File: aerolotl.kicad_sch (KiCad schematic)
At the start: 0 parts

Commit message: final rev1
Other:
- sheet Igniters renamed Igniter
- sheet External ports: added PWM1, PWM2; removed none
- sheet MCU ports: added PWM1, PWM2; removed none
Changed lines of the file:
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@@
 	(bus
 		(pts
-			(xy 250.19 140.335) (xy 294.005 140.335)
+			(xy 250.19 138.43) (xy 294.005 138.43)
 		)
 		(stroke
@@
 	(bus
 		(pts
-			(xy 250.19 138.43) (xy 294.005 138.43)
+			(xy 250.19 136.525) (xy 294.005 136.525)
 		)
 		(stroke
@@
 	(wire
 		(pts
-			(xy 250.19 147.955) (xy 294.005 147.955)
+			(xy 250.19 149.225) (xy 294.005 149.225)
 		)
 		(stroke
@@
 		)
 	)
+	(wire
+		(pts
+			(xy 250.19 140.97) (xy 294.005 140.97)
+		)
+		(stroke
+			(width 0)
+			(type default)
+		)
+	)
 	(bus
 		(pts
@@
 	(wire
 		(pts
-			(xy 250.19 146.05) (xy 294.005 146.05)
+			(xy 250.19 147.32) (xy 294.005 147.32)
 		)
 		(stroke
@@
 		(pts
 			(xy 127 52.07) (xy 127 90.805)
+		)
+		(stroke
+			(width 0)
+			(type default)
+		)
+	)
+	(wire
+		(pts
+			(xy 250.19 143.51) (xy 294.005 143.51)
 		)
 		(stroke
@@
 			(color 0 0 0 0.0000)
 		)
-		(property "Sheetname" "Igniters"
+		(property "Sheetname" "Igniter"
 			(at 294.005 211.3784 0)
 			(effects
@@
 		)
 		(pin "I2C2{SDA, SCL}" bidirectional
+			(at 294.005 136.525 180)
+			(effects
+				(font
+					(size 1.27 1.27)
+				)
+				(justify left)
+			)
+		)
+		(pin "I2C4{SDA, SCL}" bidirectional
 			(at 294.005 138.43 180)
-			(effects
-				(font
-					(size 1.27 1.27)
-				)
-				(justify left)
-			)
-		)
-		(pin "I2C4{SDA, SCL}" bidirectional
-			(at 294.005 140.335 180)
 			(effects
 				(font
@@
 		)
 		(pin "USART3_TARGET_RX" input
-			(at 294.005 146.05 180)
+			(at 294.005 147.32 180)
 			(effects
 				(font
@@
 		)
 		(pin "USART3_TARGET_TX" output
-			(at 294.005 147.955 180)
+			(at 294.005 149.225 180)
+			(effects
+				(font
+					(size 1.27 1.27)
+				)
+				(justify left)
+			)
+		)
+		(pin "PWM1" input
+			(at 294.005 140.97 180)
+			(effects
+				(font
+					(size 1.27 1.27)
+				)
+				(justify left)
+			)
+		)
+		(pin "PWM2" input
+			(at 294.005 143.51 180)
 			(effects
 				(font
@@
 		)
 		(pin "I2C2{SDA, SCL}" input
+			(at 250.19 136.525 0)
+			(effects
+				(font
+					(size 1.27 1.27)
+				)
+				(justify right)
+			)
+		)
+		(pin "I2C4{SDA, SCL}" input
 			(at 250.19 138.43 0)
-			(effects
-				(font
-					(size 1.27 1.27)
-				)
-				(justify right)
-			)
-		)
-		(pin "I2C4{SDA, SCL}" input
-			(at 250.19 140.335 0)
 			(effects
 				(font
@@
 		)
 		(pin "USART3_RX" input
-			(at 250.19 146.05 0)
+			(at 250.19 147.32 0)
 			(effects
 				(font
@@
 		)
 		(pin "USART3_TX" output
-			(at 250.19 147.955 0)
+			(at 250.19 149.225 0)
 			(effects
 				(font
@@
 			(effects
 				(font
+					(size 1.27 1.27)
+				)
+				(justify right)
+			)
+		)
+		(pin "PWM1" output
+			(at 250.19 140.97 0)
+			(effects
+				(font
+					(size 1.27 1.27)
+				)
+				(justify right)
+			)
+		)
+		(pin "PWM2" output
+			(at 250.19 143.51 0)
+			(effects
+				(font

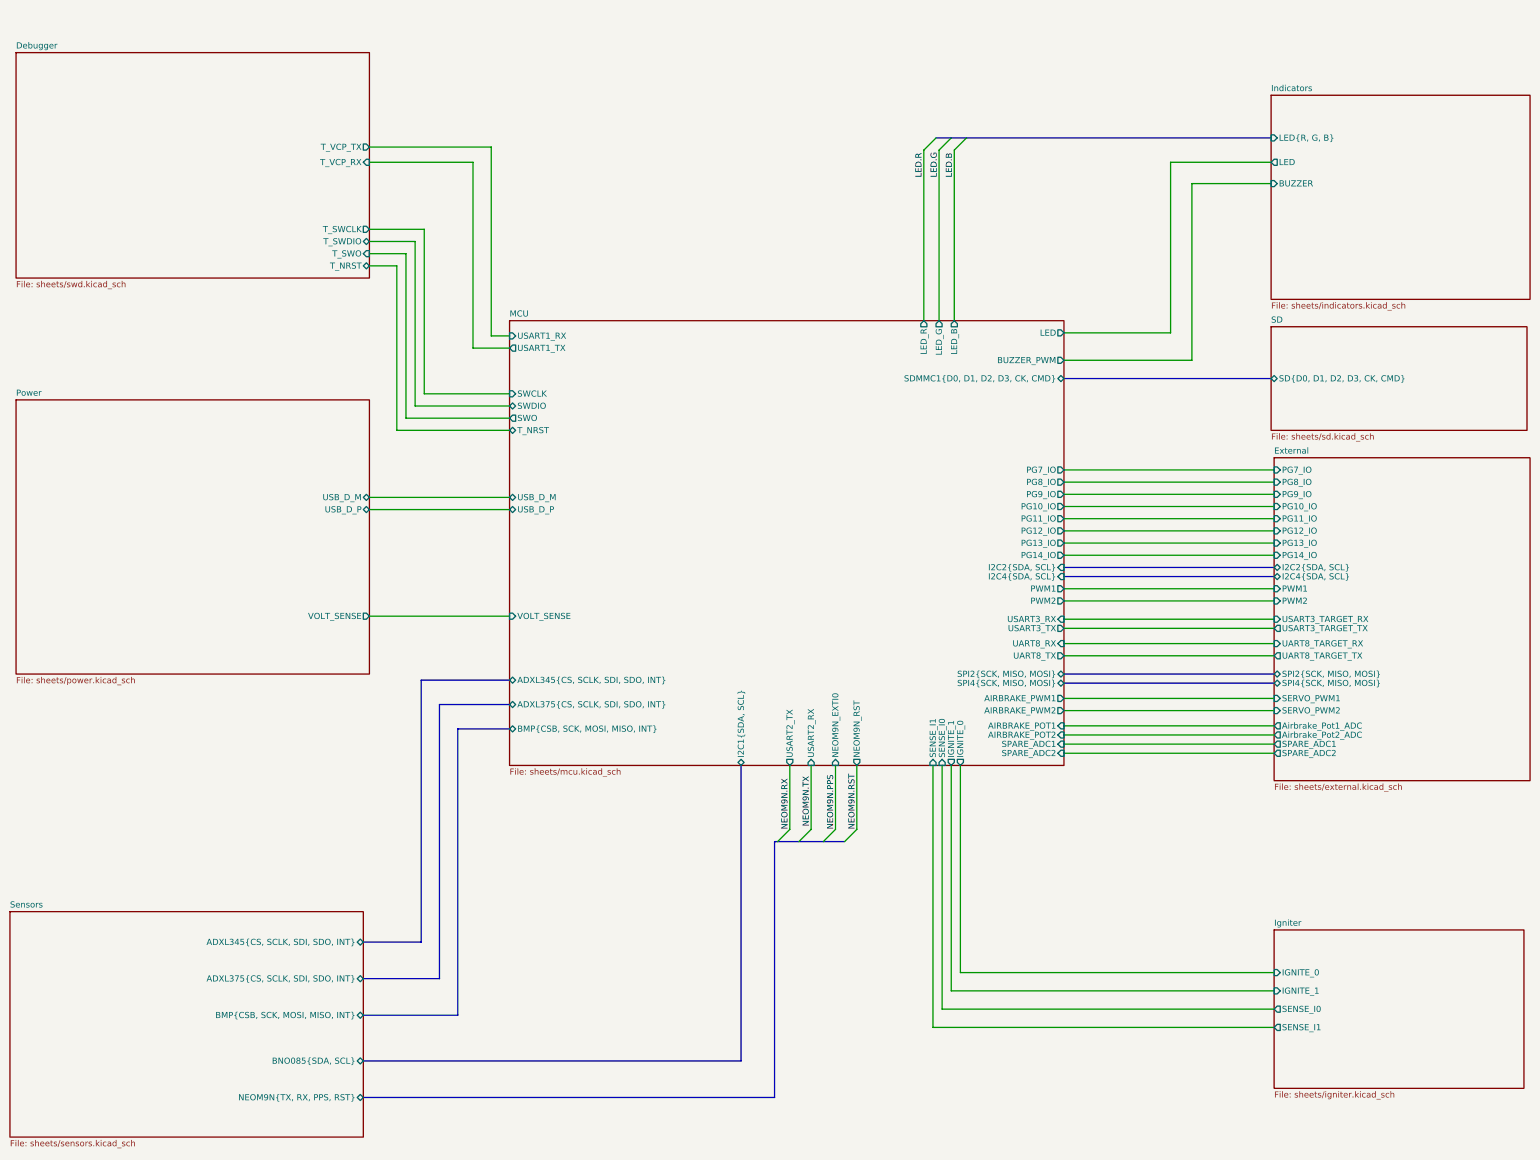
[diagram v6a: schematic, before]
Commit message: Cleared ALL ERC warnings
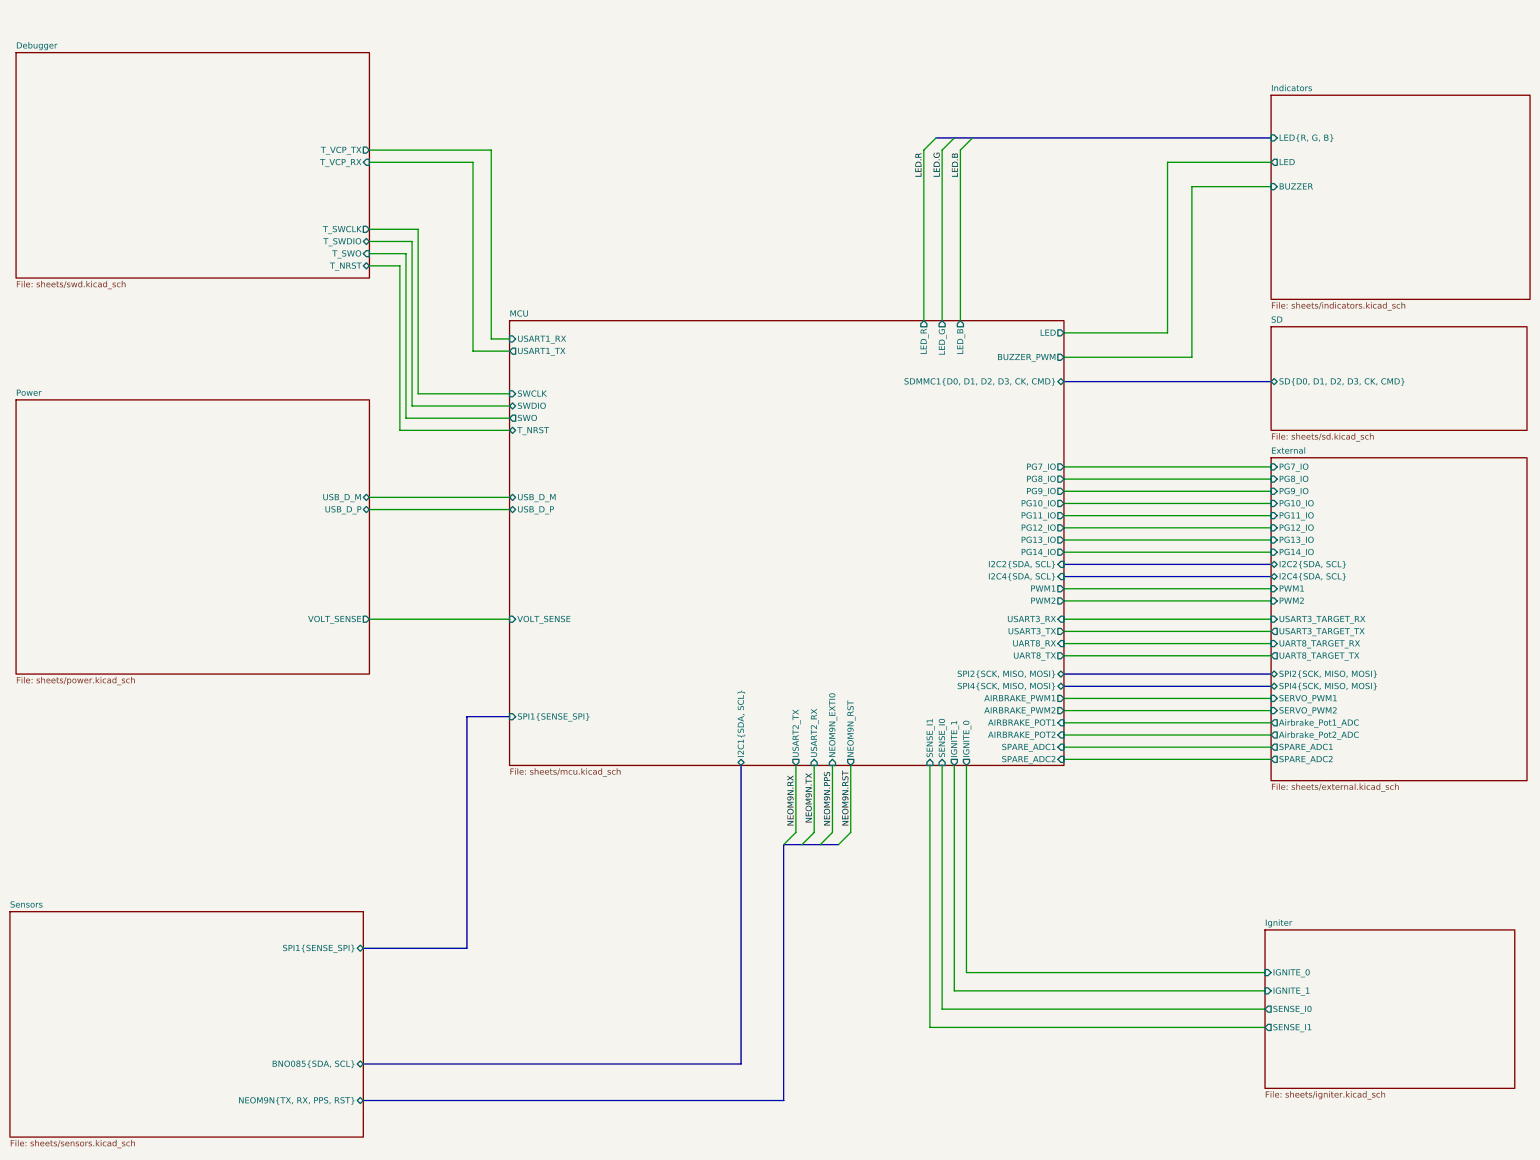
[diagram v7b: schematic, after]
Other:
- sheet MCU ports: added SPI1{SENSE_SPI}; removed ADXL345{CS, SCLK, SDI, SDO, INT}, ADXL375{CS, SCLK, SDI, SDO, INT}, BMP{CSB, SCK, MOSI, MISO, INT}
- sheet Sensors ports: added SPI1{SENSE_SPI}; removed ADXL345{CS, SCLK, SDI, SDO, INT}, ADXL375{CS, SCLK, SDI, SDO, INT}, BMP{CSB, SCK, MOSI, MISO, INT}

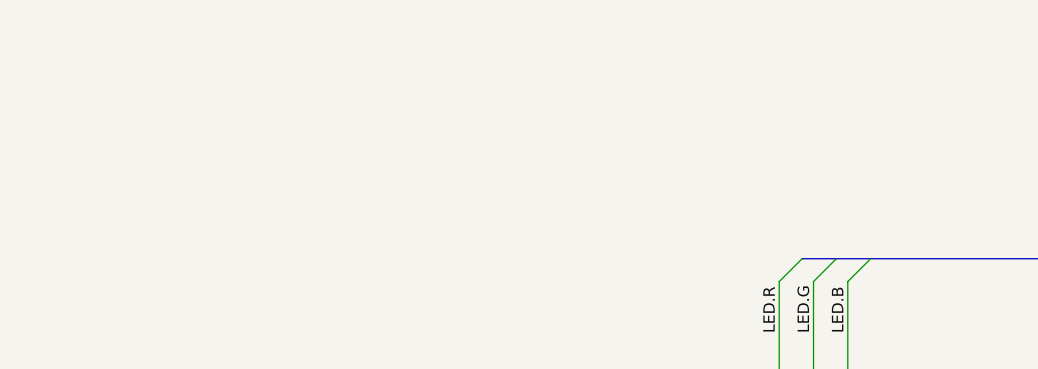
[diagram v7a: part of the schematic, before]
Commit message: letter size schematic pages formatted
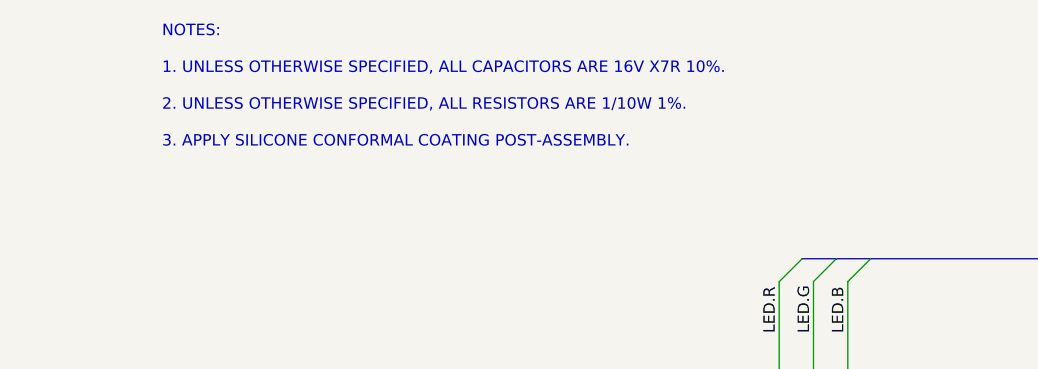
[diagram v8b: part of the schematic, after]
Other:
- note added: "NOTES: 1. UNLESS OTHERWISE SPECIFIED, ALL CAPACITORS ARE 16V X7R 10%. 2. UNLESS OTHERWISE SPECIFIED, ALL RESISTORS ARE 1/10W 1%. 3. APPLY SILICONE CONFORMAL COATING POST-ASSEMBLY."
- company: (none) -> Stanford Space Initiative
- title: (none) -> AEROLOTL NEW COLLINS FLIGHT COMPUTER
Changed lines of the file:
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@@
 	(generator_version "9.0")
 	(paper "A3")
+	(title_block
+		(title "AEROLOTL NEW COLLINS FLIGHT COMPUTER")
+		(date "2026-02-27")
+		(rev "2")
+		(company "Stanford Space Initiative")
+		(comment 1 "By KOICHI KIMOTO")
+		(comment 2 "Implemented Logan's comments")
+	)
 	(bus_alias "SENSE_SPI"
 		(members "SCK" "MISO" "MOSI" "CS_345" "CS_375" "CS_BMP" "INT_345" "INT_375"
@@
 		)
 	)
+	(text "NOTES:\n\n1. UNLESS OTHERWISE SPECIFIED, ALL CAPACITORS ARE 16V X7R 10%.\n\n2. UNLESS OTHERWISE SPECIFIED, ALL RESISTORS ARE 1/10W 1%.\n\n3. APPLY SILICONE CONFORMAL COATING POST-ASSEMBLY."
+		(exclude_from_sim no)
+		(at 152.4 27.94 0)
+		(effects
+			(font
+				(size 1.27 1.27)
+			)
+			(justify left)
+		)
+	)
